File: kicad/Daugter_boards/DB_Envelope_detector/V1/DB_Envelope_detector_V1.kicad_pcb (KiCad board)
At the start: 2 copper layers, 5 parts, among them P1 CONN_01X19, P2 CONN_01X19

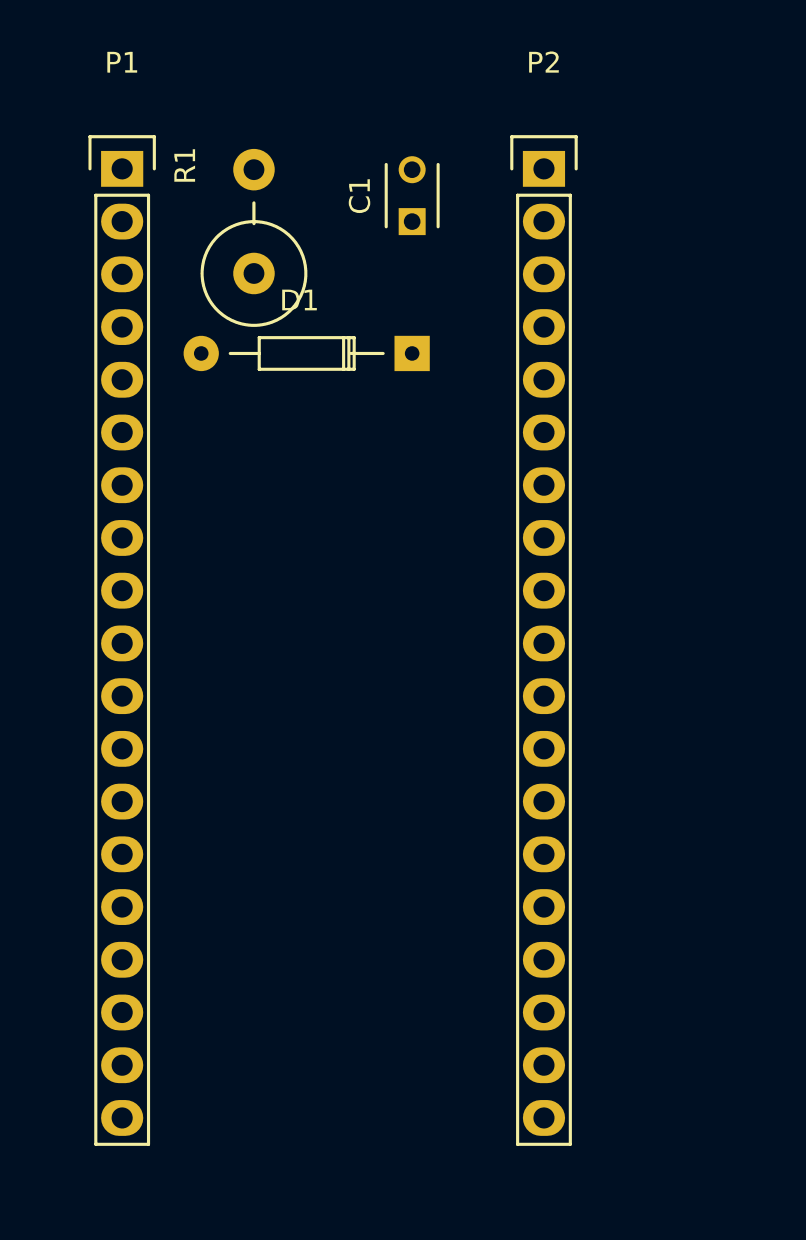
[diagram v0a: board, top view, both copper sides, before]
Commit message: adding DB_Envelope_Detector
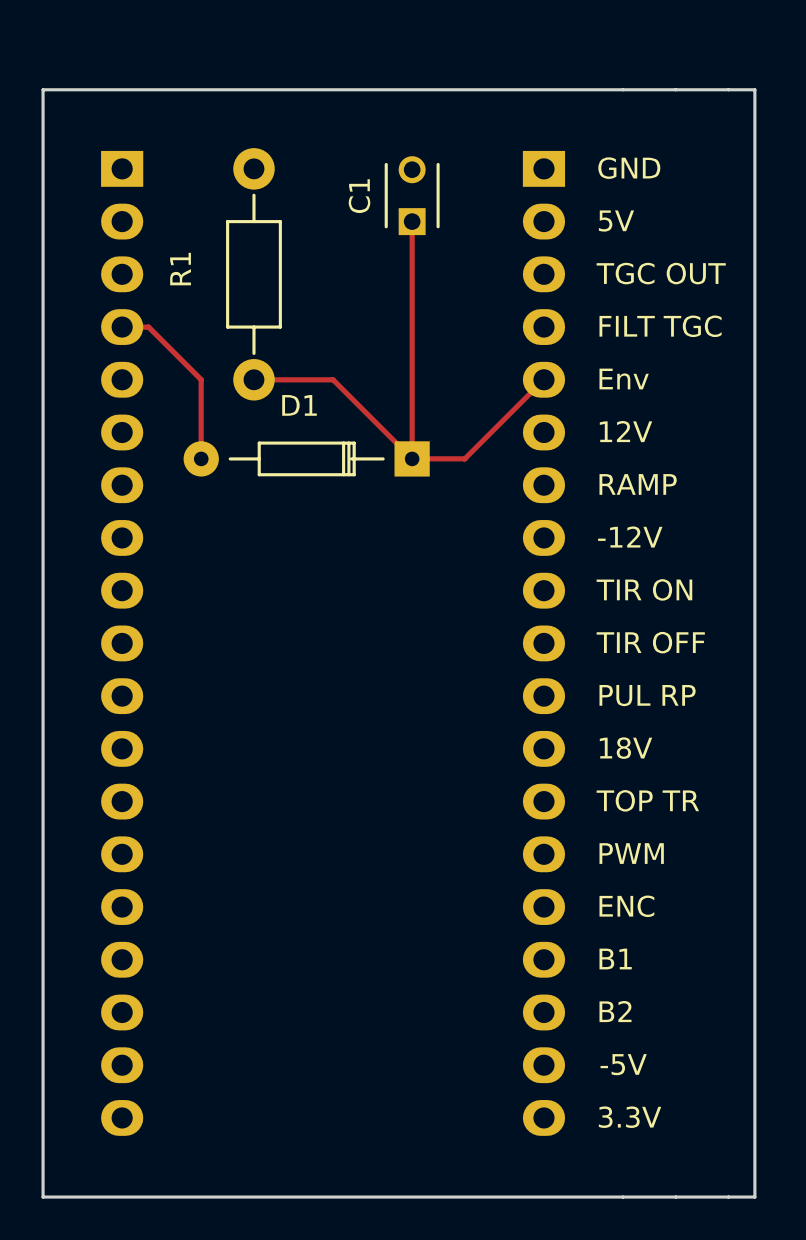
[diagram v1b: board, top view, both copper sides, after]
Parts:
- P1, P2: moved to B.Cu
- R1: footprint Resistors_ThroughHole:Resistor_Vertical_RM5mm -> Resistors_ThroughHole:Resistor_Horizontal_RM10mm
- moved R1 7.62 mm to (137.2, 115.6)
- moved D1 5.08 mm to (144.8, 119.4)
- turned P1 to 180 degrees
- turned P2 to 180 degrees
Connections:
- net Net-(C1-Pad2) renamed GND
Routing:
- net Net-(C1-Pad1): track 0.00 -> 28.6 mm
- net Net-(D1-Pad2): track 0.00 -> 8.67 mm
- added copper zone on F.Cu, net GND
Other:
- board outline added: 34.3 x 53.3 mm
- board text added: "-12V"
- board text added: "-5V"
- board text added: "12V"
- board text added: "18V"
- board text added: "3.3V"
- board text added: "5V"
- board text added: "B1"
- board text added: "B2"
- board text added: "ENC"
- board text added: "Env"
- board text added: "FILT TGC"
- board text added: "GND"
- board text added: "PUL RP"
- board text added: "PWM"
- board text added: "RAMP"
- board text added: "TGC OUT"
- board text added: "TIR OFF"
- board text added: "TIR ON"
- board text added: "TOP TR"
